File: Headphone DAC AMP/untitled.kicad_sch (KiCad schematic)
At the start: 34 parts, among them IC1 ADP7185ACPZN1.0-R7, IC2 TPS74501PDRVR, U10 TLV71x_WSON-6, U11 ADP5071AREZ-R7

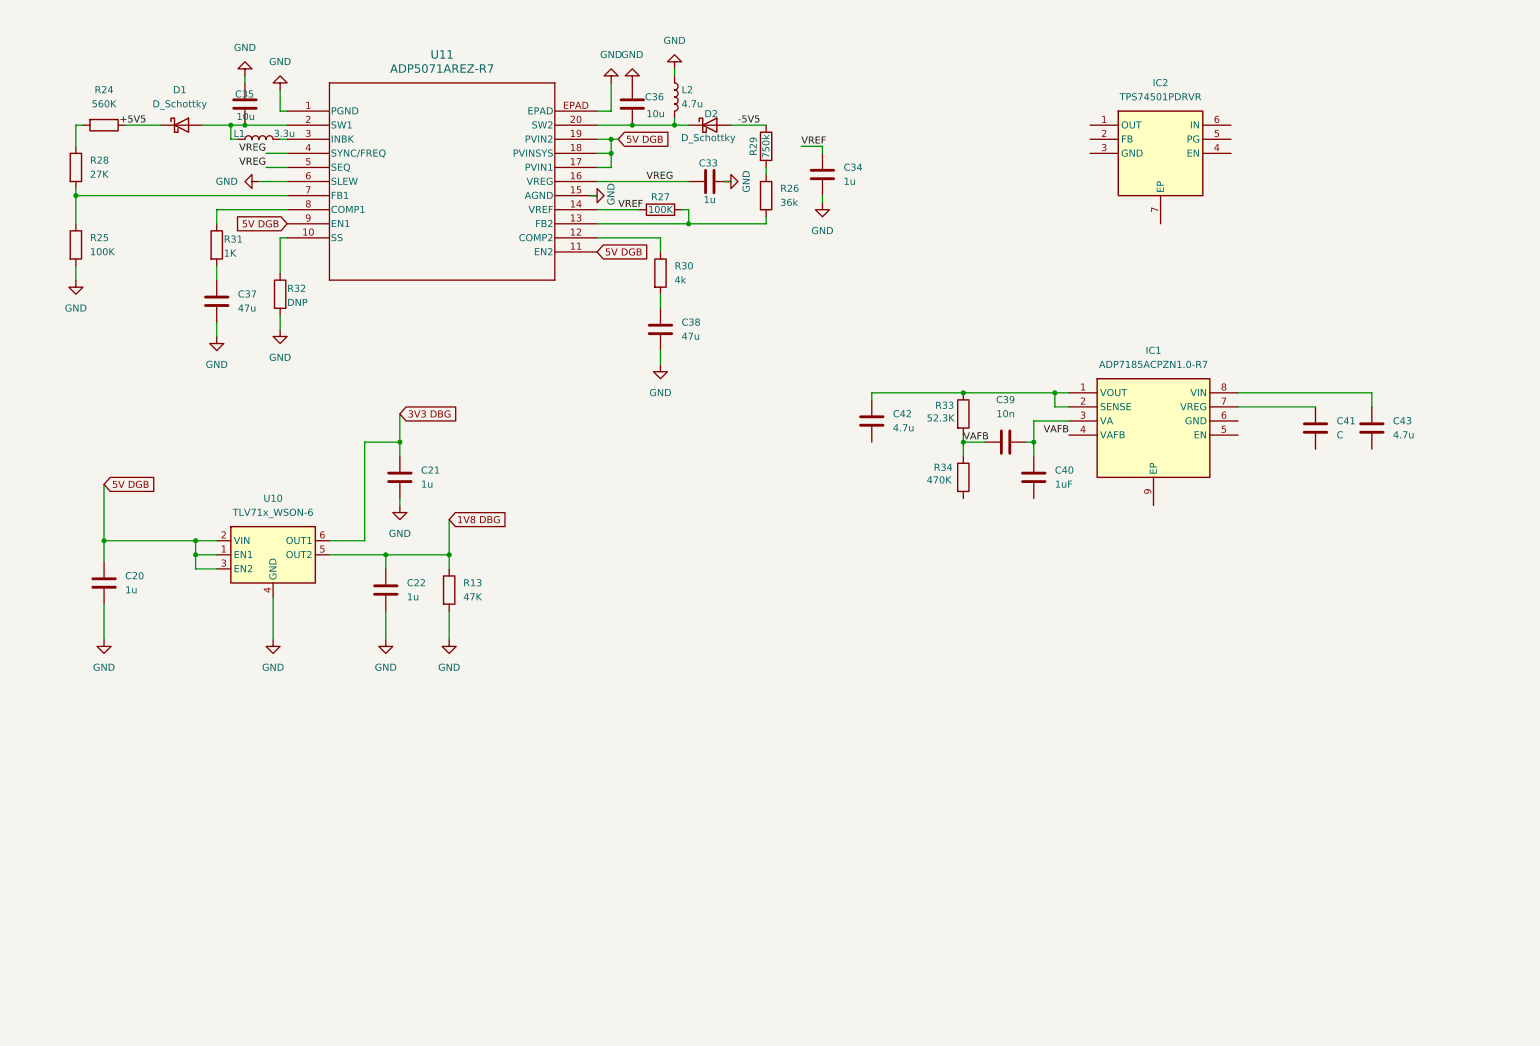
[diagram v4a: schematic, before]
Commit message: Completed a significant amount of the power and routing
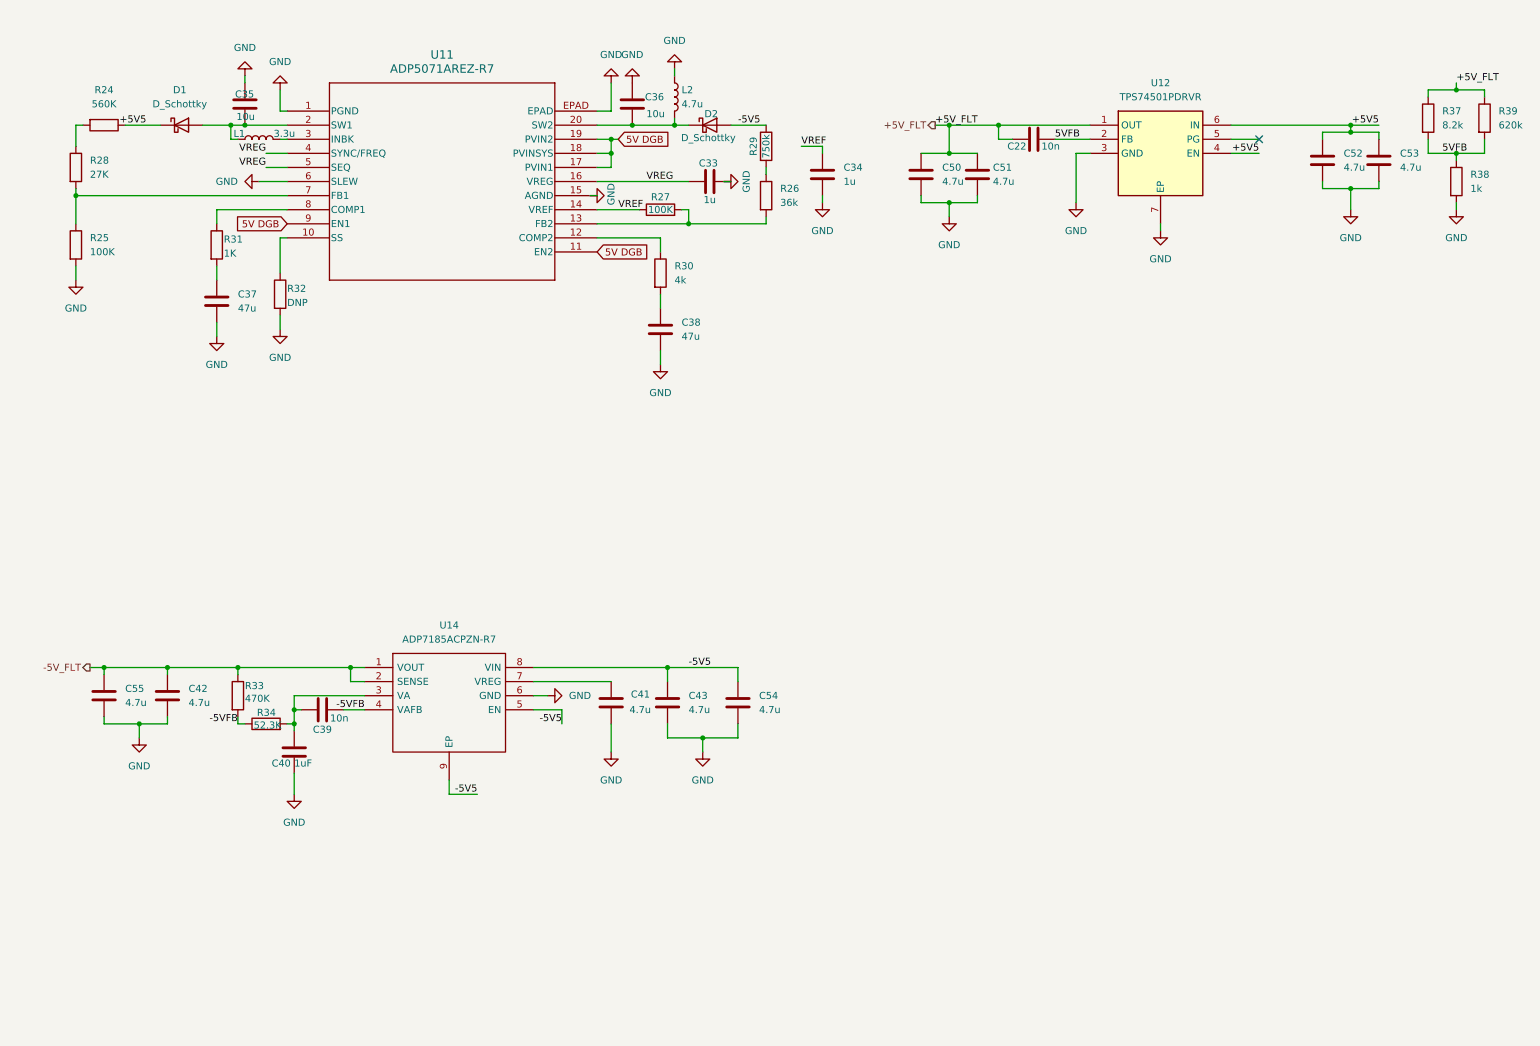
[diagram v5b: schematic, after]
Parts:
- removed C20, C21: 1u, symbol Device:C
- removed IC1: ADP7185ACPZN1.0-R7, SON50P200X200X60-9N, symbol ADP7185ACPZN1_0-R7:ADP7185ACPZN1.0-R7
- removed R13: 47K, symbol Device:R
- removed U10: TLV71x_WSON-6, Package_SON:WSON-6_1.5x1.5mm_P0.5mm, symbol Regulator_Linear:TLV71x_WSON-6
- added C50, C51, C52, C53, C54, C55: 4.7u, Capacitor_SMD:C_0805_2012Metric_Pad1.18x1.45mm_HandSolder, symbol Device:C
- added R37: 8.2k, Resistor_SMD:R_0805_2012Metric_Pad1.20x1.40mm_HandSolder, symbol Device:R
- added R38: 1k, Resistor_SMD:R_0805_2012Metric_Pad1.20x1.40mm_HandSolder, symbol Device:R
- added R39: 620k, Resistor_SMD:R_0805_2012Metric_Pad1.20x1.40mm_HandSolder, symbol Device:R
- added U14: ADP7185ACPZN-R7, SON50P200X200X60-9N, symbol ADP7185ACPZN-R7:ADP7185ACPZN-R7
- C22: value 1u -> 10n; footprint (none) -> Capacitor_SMD:C_0805_2012Metric_Pad1.18x1.45mm_HandSolder
- C33, C34, C35, C36, C37, C38, C39, C40, C42, C43, L2: footprint (none) -> Capacitor_SMD:C_0805_2012Metric_Pad1.18x1.45mm_HandSolder
- C41: value C -> 4.7u; footprint (none) -> Capacitor_SMD:C_0805_2012Metric_Pad1.18x1.45mm_HandSolder
- R24, R25, R26, R27, R28, R29, R30, R31, R32: footprint (none) -> Resistor_SMD:R_0805_2012Metric_Pad1.20x1.40mm_HandSolder
- R33: value 52.3K -> 470K; footprint (none) -> Resistor_SMD:R_0805_2012Metric_Pad1.20x1.40mm_HandSolder
- R34: value 470K -> 52.3K; footprint (none) -> Resistor_SMD:R_0805_2012Metric_Pad1.20x1.40mm_HandSolder
- renumbered IC2 to U12
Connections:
- net 1V8 DBG is gone; now on net +5V_FLT: C22.1
- net +5V5: now also U12.4 (EN), U12.6 (IN), C52.1, C53.1
- net -5V5: now also C43.1, C54.1, U14.5 (EN), U14.8 (VIN), U14.9 (EP)
- net GND: now also C40.2, C41.2, C42.2, C43.2, U12.3 (GND), U12.7 (EP), C50.2, C51.2, C52.2, C53.2, C54.2, C55.2, R38.2, U14.6 (GND); no longer C22.2
- net +5V_FLT: now reaches U12.1 (OUT)
- net +5V_FLT: now also C50.1, C51.1, R37.1, R39.1
- net 5VFB: now reaches U12.2 (FB)
- net 5VFB: now also C22.2, R37.2, R38.1, R39.2
- net at C39.2, C40.1: now also R34.2, U14.3 (VA)
- net -5V_FLT: now reaches C42.1, R33.1
- net -5V_FLT: now also C55.1, U14.1 (VOUT), U14.2 (SENSE)
- net at C41.1: now also U14.7 (VREG)
- net VAFB renamed -5VFB
- net -5VFB: now also U14.4 (VAFB)
- no-connect marks 0 -> 1
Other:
- moved on the sheet: C39, C40, C41, C42, C43, R33, R34

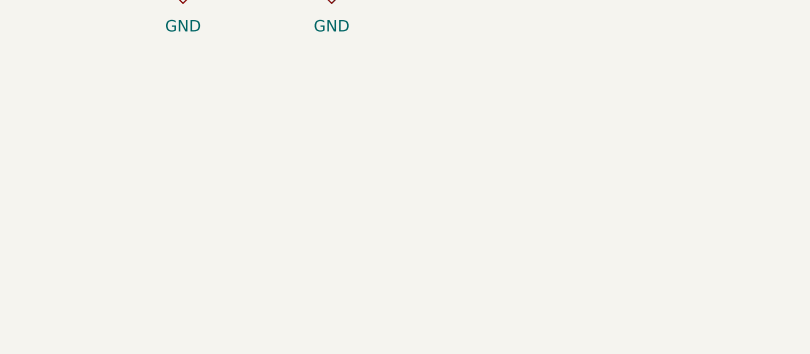
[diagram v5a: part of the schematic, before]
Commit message: Added ground and 0.9v
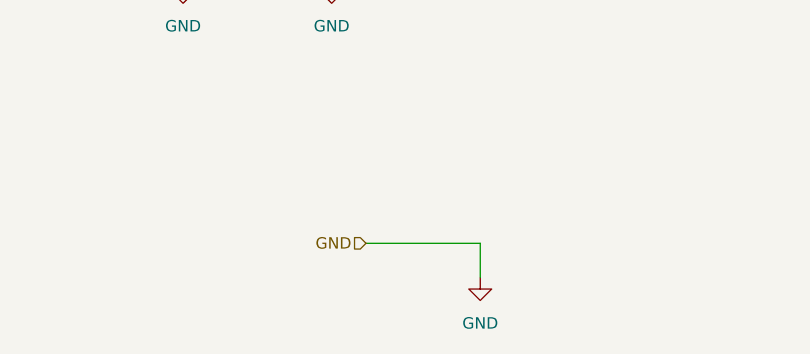
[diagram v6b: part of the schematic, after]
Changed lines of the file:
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@@
 	(wire
 		(pts
+			(xy 140.97 175.26) (xy 153.67 175.26)
+		)
+		(stroke
+			(width 0)
+			(type default)
+		)
+	)
+	(wire
+		(pts
 			(xy 54.61 24.13) (xy 54.61 25.4)
 		)
@@
 	(wire
 		(pts
+			(xy 153.67 175.26) (xy 153.67 179.07)
+		)
+		(stroke
+			(width 0)
+			(type default)
+		)
+	)
+	(wire
+		(pts
 			(xy 91.44 153.67) (xy 96.52 153.67)
 		)
@@
 		)
 	)
+	(hierarchical_label "GND"
+		(shape input)
+		(at 140.97 175.26 180)
+		(effects
+			(font
+				(size 1.27 1.27)
+			)
+			(justify right)
+		)
+	)
 	(hierarchical_label "-5V_FLT"
 		(shape output)
@@
 					(unit 1)
 				)
+			)
+		)
+	)
+	(symbol
+		(lib_id "power:GND")
+		(at 153.67 179.07 0)
+		(unit 1)
+		(exclude_from_sim no)
+		(in_bom yes)
+		(on_board yes)
+		(dnp no)
+		(fields_autoplaced yes)
+		(property "Reference" "#PWR092"
+			(at 153.67 185.42 0)
+			(effects
+				(font
+					(size 1.27 1.27)
+				)
+				(hide yes)
+			)
+		)
+		(property "Value" "GND"
+			(at 153.67 184.15 0)
+			(effects
+				(font
+					(size 1.27 1.27)
+				)
+			)
+		)
+		(property "Footprint" ""
+			(at 153.67 179.07 0)
+			(effects
+				(font
+					(size 1.27 1.27)
+				)
+				(hide yes)
+			)
+		)
+		(property "Datasheet" ""
+			(at 153.67 179.07 0)
+			(effects
+				(font
+					(size 1.27 1.27)
+				)
+				(hide yes)
+			)
+		)
+		(property "Description" "Power symbol creates a global label with name \"GND\" , ground"
+			(at 153.67 179.07 0)
+			(effects
+				(font
+					(size 1.27 1.27)
+				)
+				(hide yes)
+			)
+		)
+		(pin "1"
+		)
+		(instances
+			(project "Headphone DAC AMP"
+				(path "/d034eddd-efbc-47be-a25c-37cbfbab4cd8/22bf93f4-b6c7-483e-b255-2ccf5bc3f52b"
+					(reference "#PWR092")
+					(unit 1)
+				)

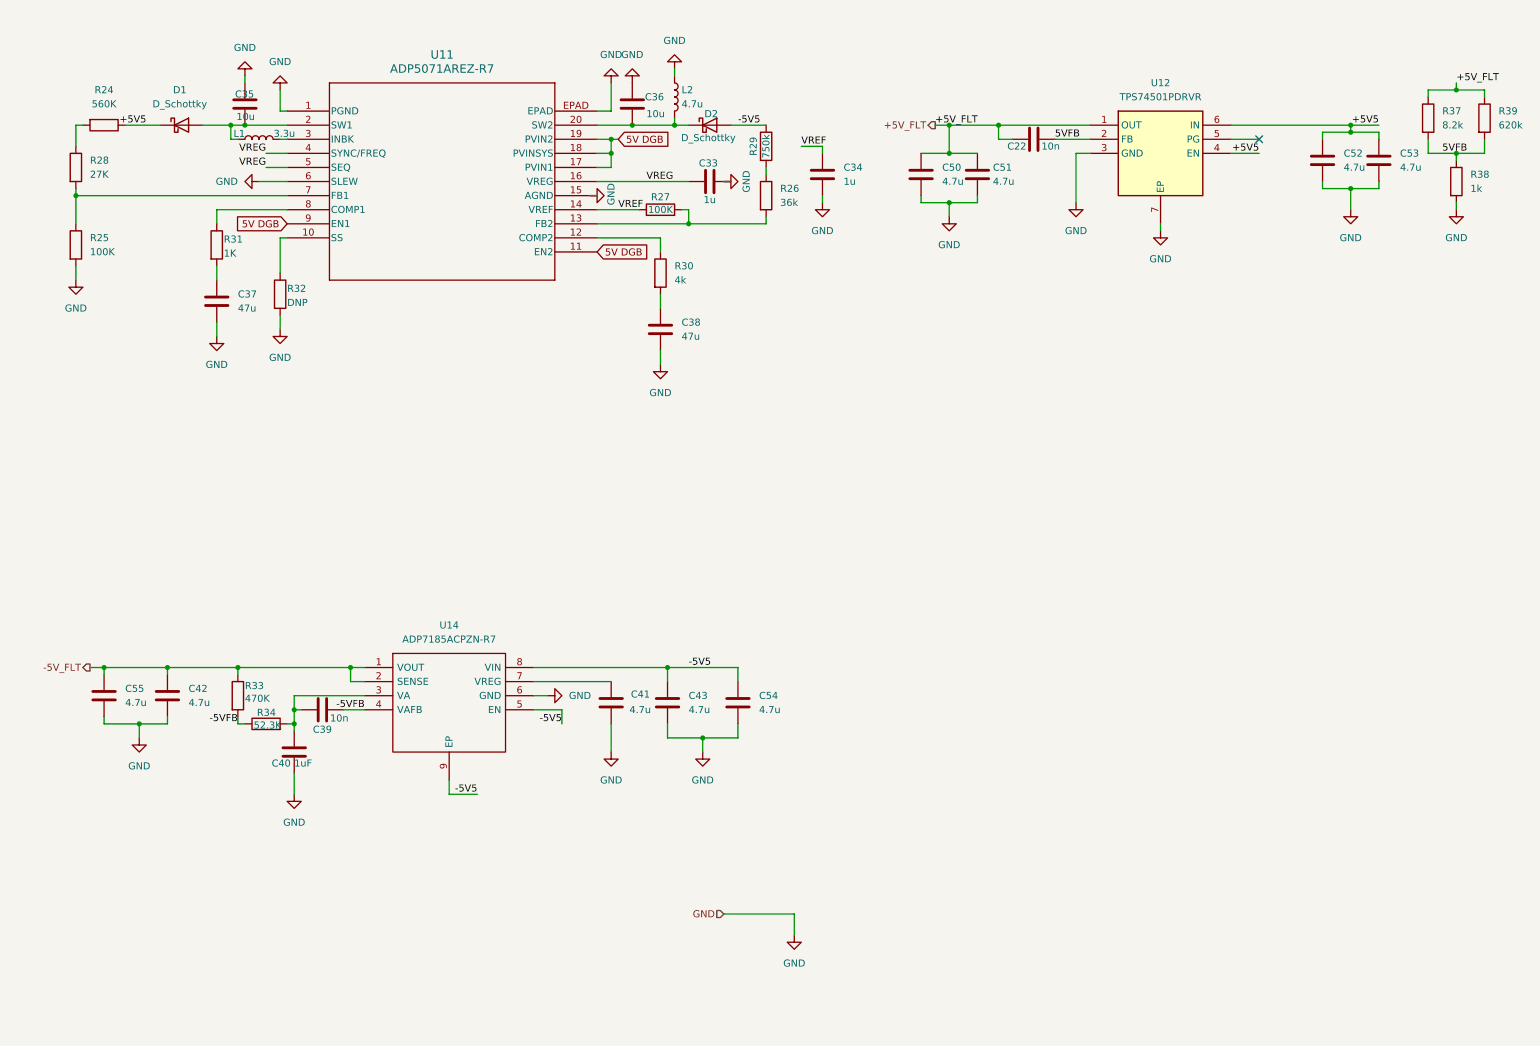
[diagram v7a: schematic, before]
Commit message: Polished DAC GPIOs and connected to XMOS
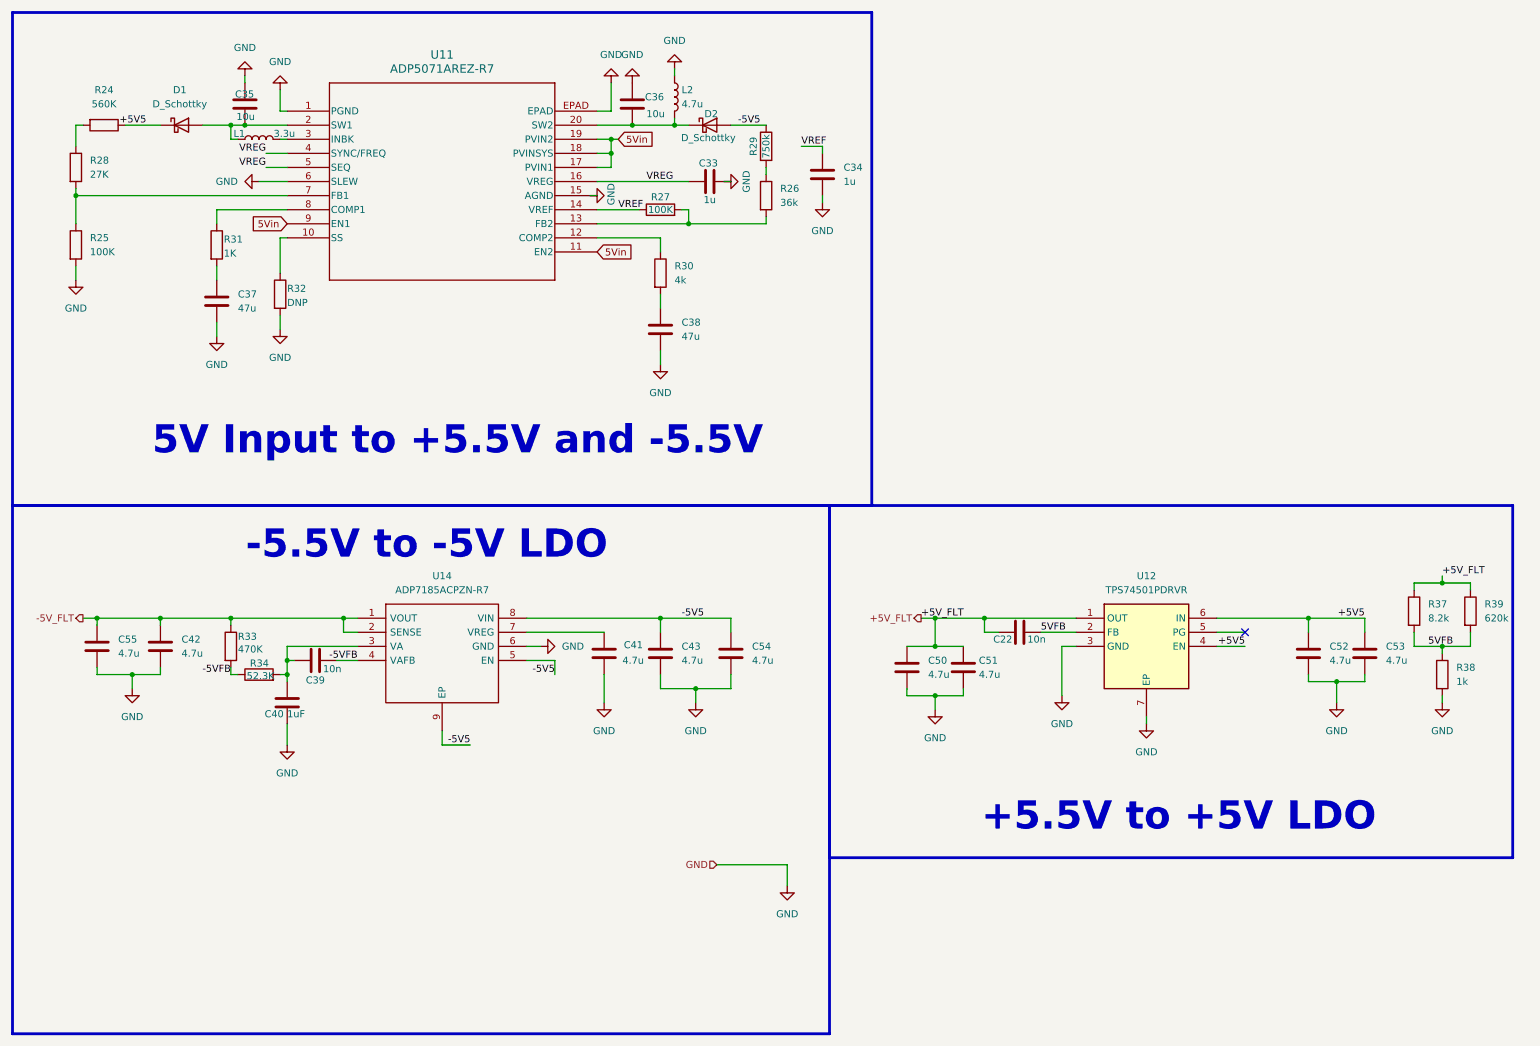
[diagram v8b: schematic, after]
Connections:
- net 5V DGB renamed 5Vin
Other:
- note added: "+5.5V to +5V LDO"
- note added: "-5.5V to -5V LDO"
- note added: "5V Input to +5.5V and -5.5V"
- moved on the sheet: C22, C39, C40, C41, C42, C43, C50, C51, C52, C53, C54, C55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
